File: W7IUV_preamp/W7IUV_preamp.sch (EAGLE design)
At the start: 30 parts, among them K1 G5L, Q1 2N2219A

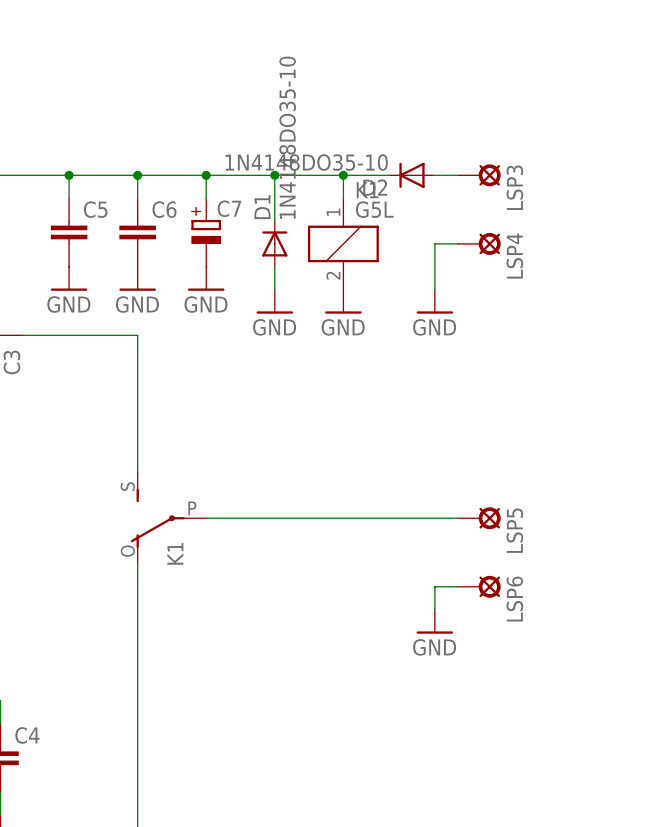
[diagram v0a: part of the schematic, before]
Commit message: Adding bypass cap
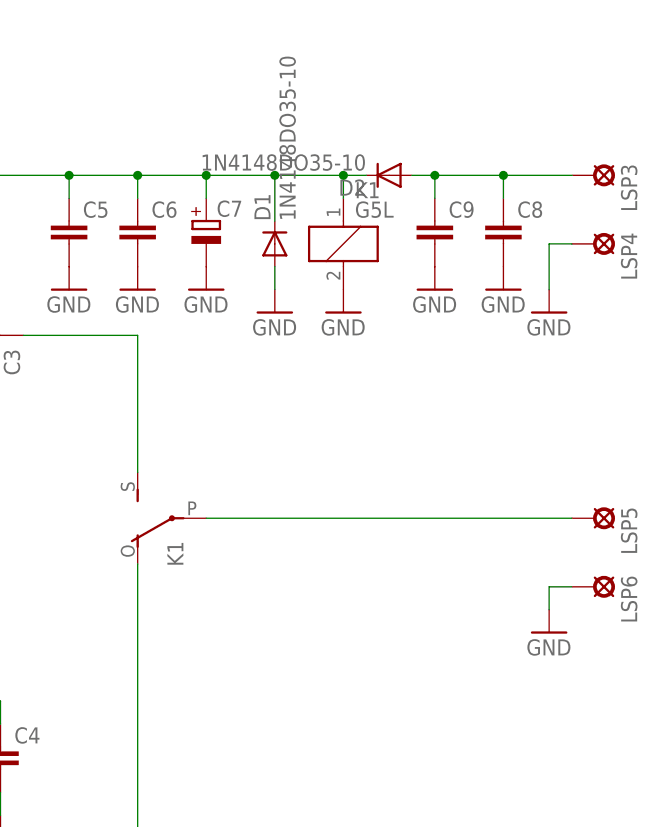
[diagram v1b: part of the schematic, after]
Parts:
- added C8, C9: (no value), rcl:C-EUC1206
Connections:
- net GND: now also C8.2, C9.2
- net N$11: now also C8.1, C9.1
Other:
- moved on the sheet: D2, LSP3, LSP4, LSP5, LSP6
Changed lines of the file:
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@@
 <part name="R5" library="rcl" deviceset="R-US_" device="M1206"/>
 <part name="GND4" library="supply1" deviceset="GND" device=""/>
+<part name="C8" library="rcl" deviceset="C-EU" device="C1206"/>
+<part name="C9" library="rcl" deviceset="C-EU" device="C1206"/>
+<part name="GND14" library="supply1" deviceset="GND" device=""/>
+<part name="GND15" library="supply1" deviceset="GND" device=""/>
 </parts>
 <sheets>
@@
 <instance part="K1" gate="2" x="119.38" y="73.66" rot="MR270"/>
 <instance part="GND11" gate="1" x="137.16" y="96.52"/>
-<instance part="LSP4" gate="G$1" x="152.4" y="104.14" rot="R270"/>
-<instance part="LSP3" gate="G$1" x="152.4" y="111.76" rot="R270"/>
-<instance part="LSP5" gate="G$1" x="152.4" y="73.66" rot="R270"/>
-<instance part="LSP6" gate="G$1" x="152.4" y="66.04" rot="R270"/>
+<instance part="LSP4" gate="G$1" x="165.1" y="104.14" rot="R270"/>
+<instance part="LSP3" gate="G$1" x="165.1" y="111.76" rot="R270"/>
+<instance part="LSP5" gate="G$1" x="165.1" y="73.66" rot="R270"/>
+<instance part="LSP6" gate="G$1" x="165.1" y="66.04" rot="R270"/>
 <instance part="LSP1" gate="G$1" x="27.94" y="73.66" rot="R90"/>
 <instance part="LSP2" gate="G$1" x="27.94" y="66.04" rot="R90"/>
 <instance part="GND1" gate="1" x="33.02" y="60.96"/>
-<instance part="GND13" gate="1" x="147.32" y="60.96"/>
-<instance part="GND12" gate="1" x="147.32" y="96.52"/>
+<instance part="GND13" gate="1" x="160.02" y="60.96"/>
+<instance part="GND12" gate="1" x="160.02" y="96.52"/>
 <instance part="FRAME1" gate="G$1" x="0" y="0"/>
 <instance part="D1" gate="G$1" x="129.54" y="104.14" rot="R90"/>
-<instance part="D2" gate="G$1" x="144.78" y="111.76" rot="R180"/>
+<instance part="D2" gate="G$1" x="142.24" y="111.76" rot="R180"/>
 <instance part="GND10" gate="1" x="129.54" y="96.52"/>
 <instance part="H1" gate="G$1" x="40.64" y="116.84"/>
@@
 <instance part="R5" gate="G$1" x="78.74" y="45.72" rot="R270"/>
 <instance part="GND4" gate="1" x="78.74" y="38.1"/>
+<instance part="C8" gate="G$1" x="154.94" y="106.68"/>
+<instance part="C9" gate="G$1" x="147.32" y="106.68"/>
+<instance part="GND14" gate="1" x="147.32" y="99.06"/>
+<instance part="GND15" gate="1" x="154.94" y="99.06"/>
 </instances>
 <busses>
@@
 <pinref part="LSP6" gate="G$1" pin="MP"/>
 <pinref part="GND13" gate="1" pin="GND"/>
-<wire x1="149.86" y1="66.04" x2="147.32" y2="66.04" width="0.1524" layer="91"/>
-<wire x1="147.32" y1="66.04" x2="147.32" y2="63.5" width="0.1524" layer="91"/>
+<wire x1="162.56" y1="66.04" x2="160.02" y2="66.04" width="0.1524" layer="91"/>
+<wire x1="160.02" y1="66.04" x2="160.02" y2="63.5" width="0.1524" layer="91"/>
 </segment>
 <segment>
@@
 <pinref part="LSP4" gate="G$1" pin="MP"/>
 <pinref part="GND12" gate="1" pin="GND"/>
-<wire x1="149.86" y1="104.14" x2="147.32" y2="104.14" width="0.1524" layer="91"/>
-<wire x1="147.32" y1="104.14" x2="147.32" y2="99.06" width="0.1524" layer="91"/>
+<wire x1="162.56" y1="104.14" x2="160.02" y2="104.14" width="0.1524" layer="91"/>
+<wire x1="160.02" y1="104.14" x2="160.02" y2="99.06" width="0.1524" layer="91"/>
 </segment>
 <segment>
@@
 <pinref part="GND4" gate="1" pin="GND"/>
 </segment>
+<segment>
+<pinref part="C9" gate="G$1" pin="2"/>
+<pinref part="GND14" gate="1" pin="GND"/>
+</segment>
+<segment>
+<pinref part="C8" gate="G$1" pin="2"/>
+<pinref part="GND15" gate="1" pin="GND"/>
+</segment>
 </net>
 <net name="N$2" class="0">
@@
 <pinref part="K1" gate="2" pin="P"/>
 <pinref part="LSP5" gate="G$1" pin="MP"/>
-<wire x1="121.92" y1="73.66" x2="149.86" y2="73.66" width="0.1524" layer="91"/>
+<wire x1="121.92" y1="73.66" x2="162.56" y2="73.66" width="0.1524" layer="91"/>
 </segment>
 </net>
@@
 <junction x="129.54" y="111.76"/>
 <pinref part="D2" gate="G$1" pin="C"/>
-<wire x1="142.24" y1="111.76" x2="137.16" y2="111.76" width="0.1524" layer="91"/>
+<wire x1="139.7" y1="111.76" x2="137.16" y2="111.76" width="0.1524" layer="91"/>
 <junction x="137.16" y="111.76"/>
 <pinref part="C5" gate="G$1" pin="1"/>
@@
 <pinref part="D2" gate="G$1" pin="A"/>
 <pinref part="LSP3" gate="G$1" pin="MP"/>
-<wire x1="147.32" y1="111.76" x2="149.86" y2="111.76" width="0.1524" layer="91"/>
-</segment>
-</net>
+<wire x1="144.78" y1="111.76" x2="147.32" y2="111.76" width="0.1524" layer="91"/>
+<pinref part="C9" gate="G$1" pin="1"/>
+<wire x1="147.32" y1="111.76" x2="154.94" y2="111.76" width="0.1524" layer="91"/>
+<wire x1="154.94" y1="111.76" x2="162.56" y2="111.76" width="0.1524" layer="91"/>
+<wire x1="147.32" y1="109.22" x2="147.32" y2="111.76" width="0.1524" layer="91"/>
+<junction x="147.32" y="111.76"/>
+<pinref part="C8" gate="G$1" pin="1"/>
+<wire x1="154.94" y1="109.22" x2="154.94" y2="111.76" width="0.1524" layer="91"/>
+<junction x="154.94" y="111.76"/>
+</segment>
+</net>
